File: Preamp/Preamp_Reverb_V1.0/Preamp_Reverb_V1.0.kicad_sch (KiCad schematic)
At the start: 121 parts, among them J1 Send, J2 Return, J3 Return, J4 Send, J5 Send, SW1 Pull Pot, SW2 Pull Pot, SW3 Pull Pot, SW4 Pull Pot, SW5 Pull Pot, SW6 Pull Pot, SW7 SW_SP3T, SW8 Pull Pot, SW9 Pull Pot, T1 Mesa 550185

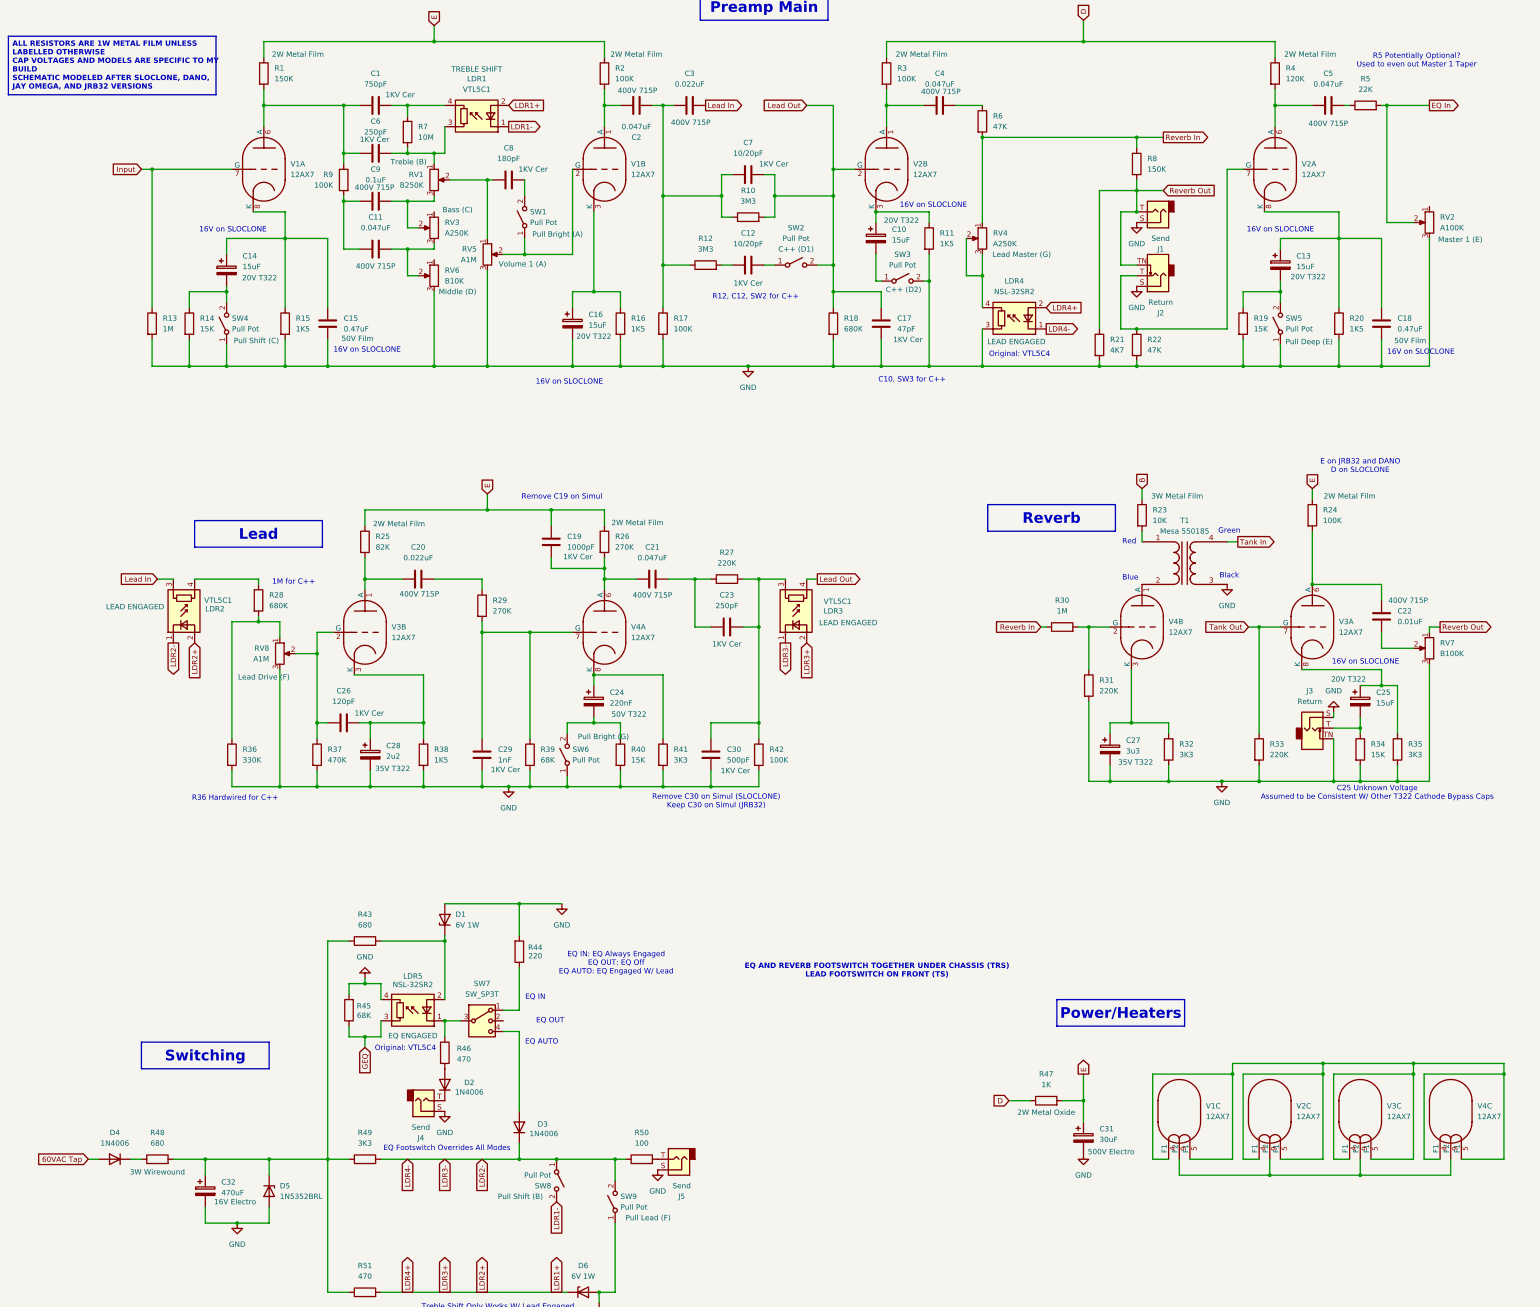
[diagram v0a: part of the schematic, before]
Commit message: Added test points to preamp board for layout planning
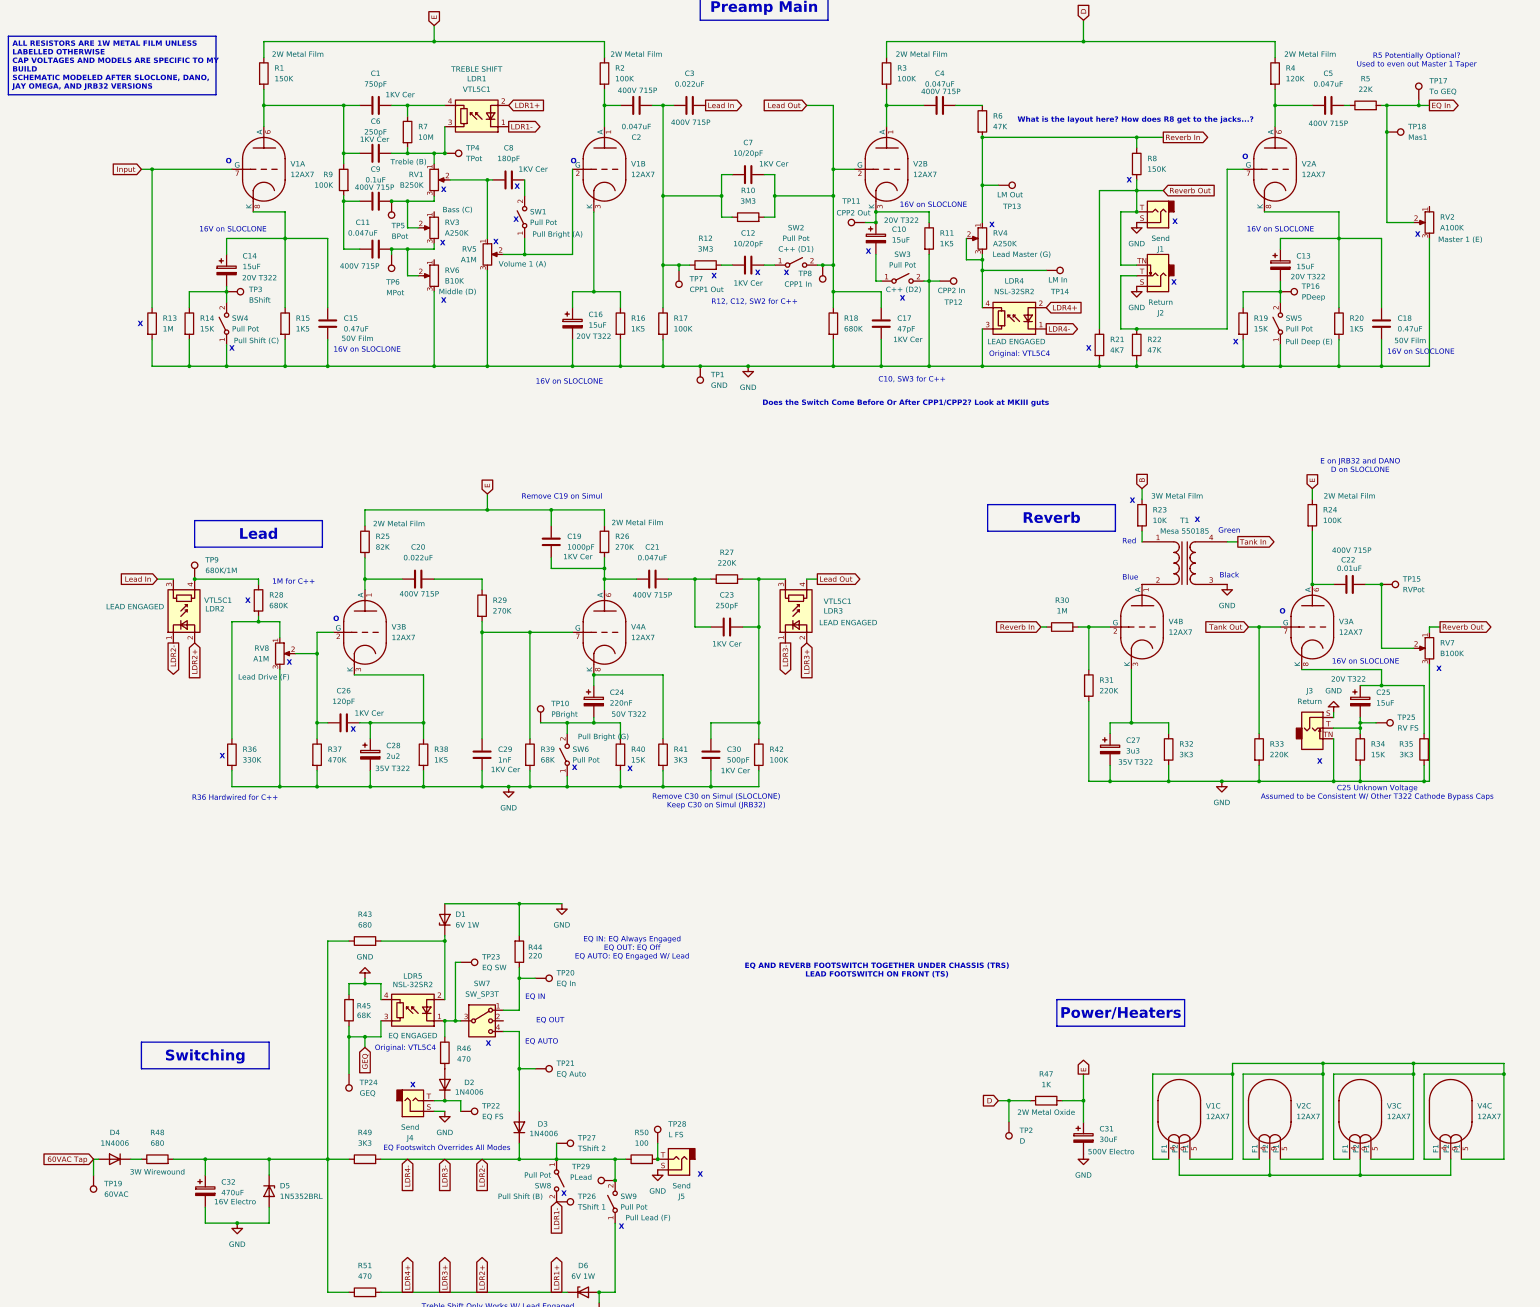
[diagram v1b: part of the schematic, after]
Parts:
- added TP1: GND, HiroFootprints:Out_Hole_3.4_1.8, symbol Connector:TestPoint
- added TP10: PBright, HiroFootprints:Out_Hole_3.4_1.8, symbol Connector:TestPoint
- added TP11: CPP2 Out, HiroFootprints:Out_Hole_3.4_1.8, symbol Connector:TestPoint
- added TP12: CPP2 In, HiroFootprints:Out_Hole_3.4_1.8, symbol Connector:TestPoint
- added TP13: LM Out, HiroFootprints:Out_Hole_3.4_1.8, symbol Connector:TestPoint
- added TP14: LM In, HiroFootprints:Out_Hole_3.4_1.8, symbol Connector:TestPoint
- added TP15: RVPot, HiroFootprints:Out_Hole_3.4_1.8, symbol Connector:TestPoint
- added TP16: PDeep, HiroFootprints:Out_Hole_3.4_1.8, symbol Connector:TestPoint
- added TP17: To GEQ, HiroFootprints:Out_Hole_3.4_1.8, symbol Connector:TestPoint
- added TP18: Mas1, HiroFootprints:Out_Hole_3.4_1.8, symbol Connector:TestPoint
- added TP19: 60VAC, HiroFootprints:Out_Hole_3.4_1.8, symbol Connector:TestPoint
- added TP2: D, HiroFootprints:Out_Hole_3.4_1.8, symbol Connector:TestPoint
- added TP20: EQ In, HiroFootprints:Out_Hole_3.4_1.8, symbol Connector:TestPoint
- added TP21: EQ Auto, HiroFootprints:Out_Hole_3.4_1.8, symbol Connector:TestPoint
- added TP22: EQ FS, HiroFootprints:Out_Hole_3.4_1.8, symbol Connector:TestPoint
- added TP23: EQ SW, HiroFootprints:Out_Hole_3.4_1.8, symbol Connector:TestPoint
- added TP24: GEQ, HiroFootprints:Out_Hole_3.4_1.8, symbol Connector:TestPoint
- added TP25: RV FS, HiroFootprints:Out_Hole_3.4_1.8, symbol Connector:TestPoint
- added TP26: TShift 1, HiroFootprints:Out_Hole_3.4_1.8, symbol Connector:TestPoint
- added TP27: TShift 2, HiroFootprints:Out_Hole_3.4_1.8, symbol Connector:TestPoint
- added TP28: L FS, HiroFootprints:Out_Hole_3.4_1.8, symbol Connector:TestPoint
- added TP29: PLead, HiroFootprints:Out_Hole_3.4_1.8, symbol Connector:TestPoint
- added TP3: BShift, HiroFootprints:Out_Hole_3.4_1.8, symbol Connector:TestPoint
- added TP4: TPot, HiroFootprints:Out_Hole_3.4_1.8, symbol Connector:TestPoint
- added TP5: BPot, HiroFootprints:Out_Hole_3.4_1.8, symbol Connector:TestPoint
- added TP6: MPot, HiroFootprints:Out_Hole_3.4_1.8, symbol Connector:TestPoint
- added TP7: CPP1 Out, HiroFootprints:Out_Hole_3.4_1.8, symbol Connector:TestPoint
- added TP8: CPP1 In, HiroFootprints:Out_Hole_3.4_1.8, symbol Connector:TestPoint
- added TP9: 680K/1M, HiroFootprints:Out_Hole_3.4_1.8, symbol Connector:TestPoint
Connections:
- net 60VAC Tap: now also TP19.1
- net D: now also TP2.1
- net EQ In: now also TP17.1, TP18.1
- net GEQ: now also TP24.1
- net GND: now also TP1.1, TP12.1
- net LDR1-: now also TP26.1
- net LDR2-: now also TP27.1, TP29.1
- net Lead Out: now also TP8.1
- net Reverb In: now also TP13.1
- net at J5.T, R50.2: now also TP28.1
- net at C25.2, J3.T, R34.1: now also TP25.1
- net at C2.2, C3.1, C7.1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: now also TP7.1
- net at C24.2, R40.1, SW6.2 (B): now also TP10.1
- net at C9.2, RV1.3, RV3.2: now also TP5.1
- net at C11.2, RV3.3, RV6.2: now also TP6.1
- net at C6.2, LDR1.3, R7.2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: now also TP4.1
- net at LDR5.1 (-), R46.1, SW7.3: now also TP23.1
- net at LDR4.4, RV4.2, RV4.3: now also TP14.1
- net at C22.2, RV7.2: now also TP15.1
- net at D2.1 (K), J4.T: now also TP22.1
- net at C14.2, R14.1, SW4.2 (B): now also TP3.1
- net at R44.1, SW7.1: now also TP20.1
- net at D3.2 (A), SW7.4: now also TP21.1
- net at C10.1, R11.1, V2.3 (K): now also TP11.1
- net at C13.2, R19.1, SW5.2 (B): now also TP16.1
- net at LDR2.4, R28.1: now also TP9.1
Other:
- note added: "Does the Switch Come Before Or After CPP1/CPP2? Look at MKIII guts"
- note added: "O"
- note added: "What is the layout here? How does R8 get to the jacks...?"
- note added: "X"
- moved on the sheet: C22, J4, R35

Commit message: Preamp Board Progress
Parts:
- C31: footprint (none) -> Capacitor_THT:CP_Axial_L42.0mm_D26.0mm_P45.00mm_Horizontal
- R1, R10, R11, R14, R15, R16, R17, R18, R2, R20, R22, R24, R25, R26, R27, R29, R3, R30, R31, R32, R33, R34, R35, R37, R38, R39, R4, R41, R42, R43, R44, R45, R46, R49, R5, R50, R51, R6, R7, R9: footprint (none) -> Resistor_THT:R_Axial_DIN0411_L9.9mm_D3.6mm_P15.24mm_Horizontal
- R47: footprint (none) -> Resistor_THT:R_Axial_DIN0516_L15.5mm_D5.0mm_P20.32mm_Horizontal
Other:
- moved on the sheet: RV7
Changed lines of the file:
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@@
 	(wire
 		(pts
-			(xy 408.94 199.39) (xy 408.94 227.33)
+			(xy 417.83 199.39) (xy 417.83 227.33)
 		)
 		(stroke
@@
 	(wire
 		(pts
-			(xy 408.94 227.33) (xy 407.67 227.33)
+			(xy 417.83 227.33) (xy 407.67 227.33)
 		)
 		(stroke
@@
 	(wire
 		(pts
-			(xy 408.94 191.77) (xy 408.94 190.5)
+			(xy 417.83 191.77) (xy 417.83 190.5)
 		)
 		(stroke
@@
 	(wire
 		(pts
-			(xy 397.51 195.58) (xy 405.13 195.58)
+			(xy 397.51 195.58) (xy 414.02 195.58)
 		)
 		(stroke
@@
 	(wire
 		(pts
-			(xy 408.94 190.5) (xy 411.48 190.5)
+			(xy 417.83 190.5) (xy 420.37 190.5)
 		)
 		(stroke
@@
 	(global_label "Reverb Out"
 		(shape output)
-		(at 411.48 190.5 0)
+		(at 420.37 190.5 0)
 		(fields_autoplaced yes)
 		(effects
@@
 		)
 		(property "Intersheetrefs" "${INTERSHEET_REFS}"
-			(at 424.988 190.5 0)
+			(at 433.878 190.5 0)
 			(effects
 				(font
@@
 			)
 		)
-		(property "Footprint" ""
+		(property "Footprint" "Resistor_THT:R_Axial_DIN0411_L9.9mm_D3.6mm_P15.24mm_Horizontal"
 			(at 247.142 220.98 90)
 			(effects
@@
 			)
 		)
-		(property "Footprint" ""
+		(property "Footprint" "Resistor_THT:R_Axial_DIN0411_L9.9mm_D3.6mm_P15.24mm_Horizontal"
 			(at 192.532 220.98 90)
 			(effects
@@
 			)
 		)
-		(property "Footprint" ""
+		(property "Footprint" "Resistor_THT:R_Axial_DIN0411_L9.9mm_D3.6mm_P15.24mm_Horizontal"
 			(at 210.312 170.18 90)
 			(effects
@@
 			)
 		)
-		(property "Footprint" ""
+		(property "Footprint" "Resistor_THT:R_Axial_DIN0411_L9.9mm_D3.6mm_P15.24mm_Horizontal"
 			(at 152.908 281.94 90)
 			(effects
@@
 			)
 		)
-		(property "Footprint" ""
+		(property "Footprint" "Resistor_THT:R_Axial_DIN0411_L9.9mm_D3.6mm_P15.24mm_Horizontal"
 			(at 379.222 163.83 90)
 			(effects
@@
 			)
 		)
-		(property "Footprint" ""
+		(property "Footprint" "Resistor_THT:R_Axial_DIN0411_L9.9mm_D3.6mm_P15.24mm_Horizontal"
 			(at 141.732 220.98 90)
 			(effects
@@
 			)
 		)
-		(property "Footprint" ""
+		(property "Footprint" "Resistor_THT:R_Axial_DIN0411_L9.9mm_D3.6mm_P15.24mm_Horizontal"
 			(at 172.212 292.1 90)
 			(effects
@@
 			)
 		)
-		(property "Footprint" ""
+		(property "Footprint" "Resistor_THT:R_Axial_DIN0411_L9.9mm_D3.6mm_P15.24mm_Horizontal"
 			(at 366.522 219.71 90)
 			(effects
@@
 			)
 		)
-		(property "Footprint" ""
+		(property "Footprint" "Resistor_THT:R_Axial_DIN0411_L9.9mm_D3.6mm_P15.24mm_Horizontal"
 			(at 111.252 118.11 90)
 			(effects
@@
 			)
 		)
-		(property "Footprint" ""
+		(property "Footprint" "Resistor_THT:R_Axial_DIN0411_L9.9mm_D3.6mm_P15.24mm_Horizontal"
 			(at 385.572 118.11 90)
 			(effects
@@
 			)
 		)
-		(property "Footprint" ""
+		(property "Footprint" "Resistor_THT:R_Axial_DIN0411_L9.9mm_D3.6mm_P15.24mm_Horizontal"
 			(at 370.332 58.42 90)
 			(effects
@@
 			)
 		)
-		(property "Footprint" ""
+		(property "Footprint" "Resistor_THT:R_Axial_DIN0411_L9.9mm_D3.6mm_P15.24mm_Horizontal"
 			(at 154.94 351.028 90)
 			(effects
@@
 			)
 		)
-		(property "Footprint" ""
+		(property "Footprint" "Resistor_THT:R_Axial_DIN0411_L9.9mm_D3.6mm_P15.24mm_Horizontal"
 			(at 214.122 118.11 90)
 			(effects
@@
 			)
 		)
-		(property "Footprint" ""
+		(property "Footprint" "Resistor_THT:R_Axial_DIN0411_L9.9mm_D3.6mm_P15.24mm_Horizontal"
 			(at 167.132 220.98 90)
 			(effects
@@
 			)
 		)
-		(property "Footprint" ""
+		(property "Footprint" "Resistor_THT:R_Axial_DIN0411_L9.9mm_D3.6mm_P15.24mm_Horizontal"
 			(at 390.652 219.71 90)
 			(effects
@@
 			)
 		)
-		(property "Footprint" ""
+		(property "Footprint" "Resistor_THT:R_Axial_DIN0411_L9.9mm_D3.6mm_P15.24mm_Horizontal"
 			(at 220.98 319.278 90)
 			(effects
@@
 			)
 		)
-		(property "Footprint" ""
+		(property "Footprint" "Resistor_THT:R_Axial_DIN0411_L9.9mm_D3.6mm_P15.24mm_Horizontal"
 			(at 153.162 170.18 90)
 			(effects
@@
 			)
 		)
-		(property "Footprint" ""
+		(property "Footprint" "Resistor_THT:R_Axial_DIN0411_L9.9mm_D3.6mm_P15.24mm_Horizontal"
 			(at 151.638 83.82 90)
 			(effects
@@
 			)
 		)
-		(property "Footprint" ""
+		(property "Footprint" "Resistor_THT:R_Axial_DIN0411_L9.9mm_D3.6mm_P15.24mm_Horizontal"
 			(at 224.282 118.11 90)
 			(effects
@@
 			)
 		)
-		(property "Footprint" ""
+		(property "Footprint" "Resistor_THT:R_Axial_DIN0411_L9.9mm_D3.6mm_P15.24mm_Horizontal"
 			(at 321.31 192.278 90)
 			(effects
@@
 			)
 		)
-		(property "Footprint" ""
+		(property "Footprint" "Resistor_THT:R_Axial_DIN0411_L9.9mm_D3.6mm_P15.24mm_Horizontal"
 			(at 409.448 219.71 90)
 			(effects
@@
 	(symbol
 		(lib_id "Device:R_Potentiometer")
-		(at 408.94 195.58 0)
+		(at 417.83 195.58 0)
 		(mirror y)
 		(unit 1)
@@
 		(dnp no)
 		(property "Reference" "RV7"
-			(at 411.48 194.3099 0)
+			(at 420.37 194.3099 0)
 			(effects
 				(font
@@
 		)
 		(property "Value" "B100K"
-			(at 411.48 196.8499 0)
+			(at 420.37 196.8499 0)
 			(effects
 				(font
@@
 		)
 		(property "Footprint" ""
-			(at 408.94 195.58 0)
+			(at 417.83 195.58 0)
 			(effects
 				(font
@@
 		)
 		(property "Datasheet" "~"
-			(at 408.94 195.58 0)
+			(at 417.83 195.58 0)
 			(effects
 				(font
@@
 		)
 		(property "Description" "Potentiometer"
-			(at 408.94 195.58 0)
+			(at 417.83 195.58 0)
 			(effects
 				(font
@@
 			)
 		)
-		(property "Footprint" ""
+		(property "Footprint" "Resistor_THT:R_Axial_DIN0411_L9.9mm_D3.6mm_P15.24mm_Horizontal"
 			(at 154.94 319.278 90)
 			(effects
@@
 			)
 		)
-		(property "Footprint" ""
+		(property "Footprint" "Resistor_THT:R_Axial_DIN0411_L9.9mm_D3.6mm_P15.24mm_Horizontal"
 			(at 241.3 180.848 90)
 			(effects
@@
 			)
 		)
-		(property "Footprint" ""
+		(property "Footprint" "Resistor_THT:R_Axial_DIN0411_L9.9mm_D3.6mm_P15.24mm_Horizontal"
 			(at 325.882 204.47 90)
 			(effects
@@
 			)
 		)
-		(property "Footprint" ""
+		(property "Footprint" "Resistor_THT:R_Axial_DIN0411_L9.9mm_D3.6mm_P15.24mm_Horizontal"
 			(at 189.992 267.97 90)
 			(effects
@@
 			)
 		)
-		(property "Footprint" ""
+		(property "Footprint" "Resistor_THT:R_Axial_DIN0411_L9.9mm_D3.6mm_P15.24mm_Horizontal"
 			(at 224.282 220.98 90)
 			(effects
@@
 			)
 		)
-		(property "Footprint" ""
+		(property "Footprint" "Resistor_THT:R_Axial_DIN0411_L9.9mm_D3.6mm_P15.24mm_Horizontal"
 			(at 300.482 69.85 90)
 			(effects
@@
 			)
 		)
-		(property "Footprint" ""
+		(property "Footprint" "Resistor_THT:R_Axial_DIN0411_L9.9mm_D3.6mm_P15.24mm_Horizontal"
 			(at 134.112 118.11 90)
 			(effects
@@
 			)
 		)
-		(property "Footprint" ""
+		(property "Footprint" "Resistor_THT:R_Axial_DIN0411_L9.9mm_D3.6mm_P15.24mm_Horizontal"
 			(at 344.932 219.71 90)
 			(effects
@@
 			)
 		)
-		(property "Footprint" ""
+		(property "Footprint" "Resistor_THT:R_Axial_DIN0411_L9.9mm_D3.6mm_P15.24mm_Horizontal"
 			(at 287.782 97.79 90)
 			(effects
@@
 			)
 		)
-		(property "Footprint" ""
+		(property "Footprint" "Resistor_THT:R_Axial_DIN0411_L9.9mm_D3.6mm_P15.24mm_Horizontal"
 			(at 337.312 123.19 90)
 			(effects
@@
 			)
 		)
-		(property "Footprint" ""
+		(property "Footprint" "Resistor_THT:R_Axial_DIN0411_L9.9mm_D3.6mm_P15.24mm_Horizontal"
 			(at 181.102 185.42 90)
 			(effects
@@
 			)
 		)
-		(property "Footprint" ""
+		(property "Footprint" "Resistor_THT:R_Axial_DIN0411_L9.9mm_D3.6mm_P15.24mm_Horizontal"
 			(at 393.7 67.818 90)
 			(effects
@@
 			)
 		)
-		(property "Footprint" ""
+		(property "Footprint" "Resistor_THT:R_Axial_DIN0411_L9.9mm_D3.6mm_P15.24mm_Horizontal"
 			(at 163.322 72.39 90)
 			(effects
@@
 			)
 		)
-		(property "Footprint" ""
+		(property "Footprint" "Resistor_THT:R_Axial_DIN0411_L9.9mm_D3.6mm_P15.24mm_Horizontal"
 			(at 210.312 58.42 90)
 			(effects
@@
 			)
 		)
-		(property "Footprint" ""
+		(property "Footprint" "Resistor_THT:R_Axial_DIN0411_L9.9mm_D3.6mm_P15.24mm_Horizontal"
 			(at 277.622 58.42 90)
 			(effects
@@
 			)
 		)
-		(property "Footprint" ""
+		(property "Footprint" "Resistor_THT:R_Axial_DIN0411_L9.9mm_D3.6mm_P15.24mm_Horizontal"
 			(at 154.94 267.208 90)
 			(effects
@@
 			)
 		)
-		(property "Footprint" ""
+		(property "Footprint" "Resistor_THT:R_Axial_DIN0411_L9.9mm_D3.6mm_P15.24mm_Horizontal"
 			(at 129.032 58.42 90)
 			(effects
@@
 			)
 		)
-		(property "Footprint" ""
+		(property "Footprint" "Resistor_THT:R_Axial_DIN0411_L9.9mm_D3.6mm_P15.24mm_Horizontal"
 			(at 264.922 118.11 90)
 			(effects
@@
 			)
 		)
-		(property "Footprint" ""
+		(property "Footprint" "Resistor_THT:R_Axial_DIN0411_L9.9mm_D3.6mm_P15.24mm_Horizontal"
 			(at 246.38 94.488 90)
 			(effects
@@
 			)
 		)
-		(property "Footprint" ""
+		(property "Footprint" "Capacitor_THT:CP_Axial_L42.0mm_D26.0mm_P45.00mm_Horizontal"
 			(at 327.3552 316.23 0)
 			(effects
@@
 			)
 		)
-		(property "Footprint" ""
+		(property "Footprint" "Resistor_THT:R_Axial_DIN0516_L15.5mm_D5.0mm_P20.32mm_Horizontal"
 			(at 317.5 305.308 90)
 			(effects
